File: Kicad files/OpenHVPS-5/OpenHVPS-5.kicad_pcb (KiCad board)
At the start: 2 copper layers, 40.6 x 20.8 mm, 89 parts, among them J1 Conn_01x03_Male, Q1 FQT7N10, Q2 BC846A, Q3 MMBT3906, Q4 MMBT3906, U1 MAX6008AEUR+T, U2 74HC14, U3 MAX4162, U4 CD14538BM

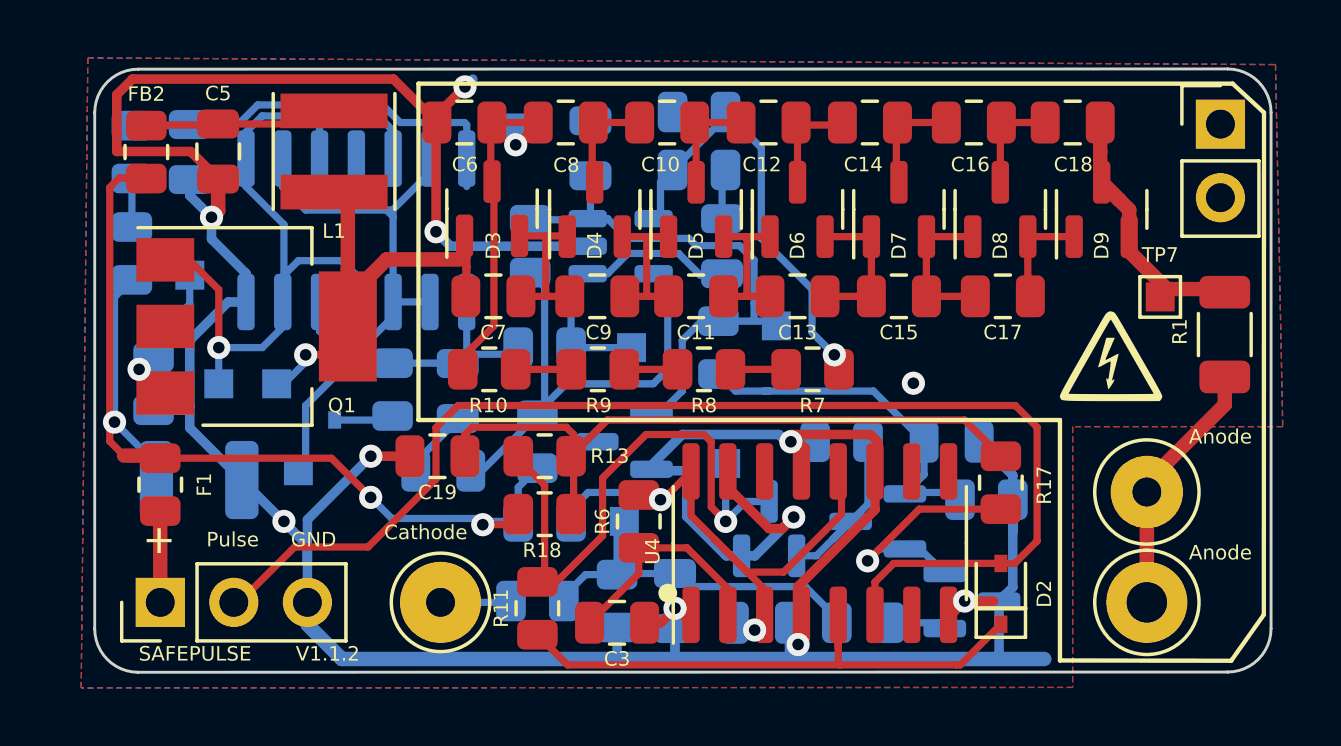
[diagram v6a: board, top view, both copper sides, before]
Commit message: Moved some lables a bit to get them centered.
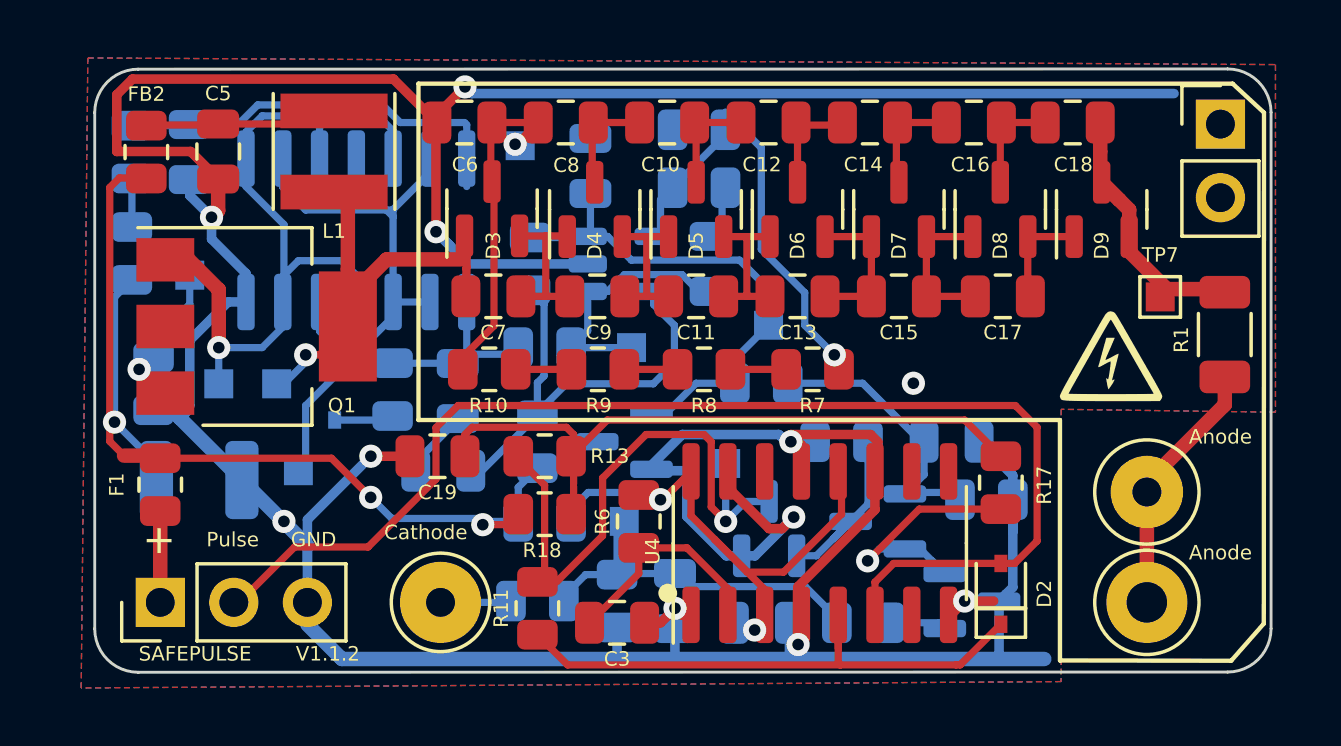
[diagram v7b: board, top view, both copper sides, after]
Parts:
- moved R14 1.92 mm to (149.2, 68.0), turned to 0 degrees
- moved C26 0.73 mm to (147.5, 63.9)
- moved C25 0.61 mm to (143.4, 60.5)
- moved R20 0.61 mm to (141.3, 63.9)
- moved R23 0.61 mm to (147.1, 59.2)
- moved R24 0.61 mm to (147.1, 61.2)
- moved TP6 0.61 mm to (140.9, 59.8)
- moved U3 0.61 mm to (144.4, 63.9)
- moved TP1 0.27 mm to (149.5, 66.0)
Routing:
- net GND: track 136.4 -> 161.5 mm
- net Net-(C24-Pad1): track 12.6 -> 9.93 mm
- net +2V5: track 19.4 -> 18.3 mm
- net Net-(C26-Pad1): track 9.77 -> 9.06 mm

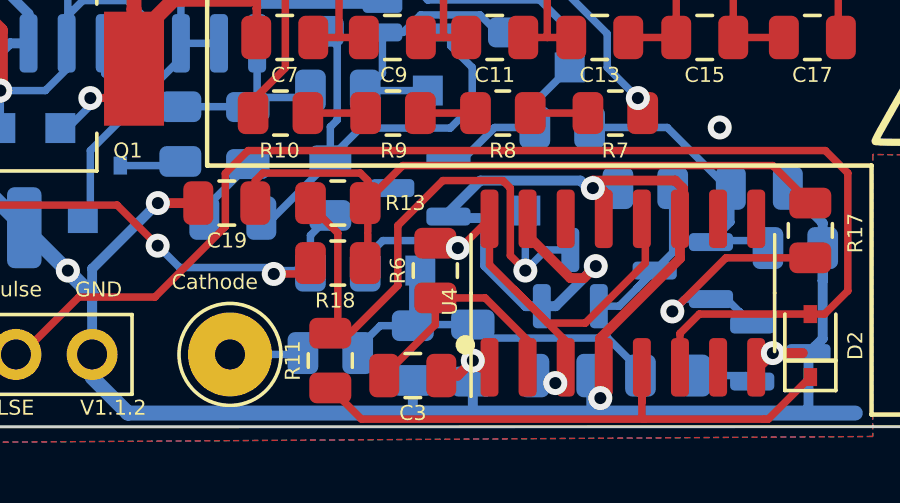
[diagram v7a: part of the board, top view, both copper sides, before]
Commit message: added digikey bom from Allan and move U4 label
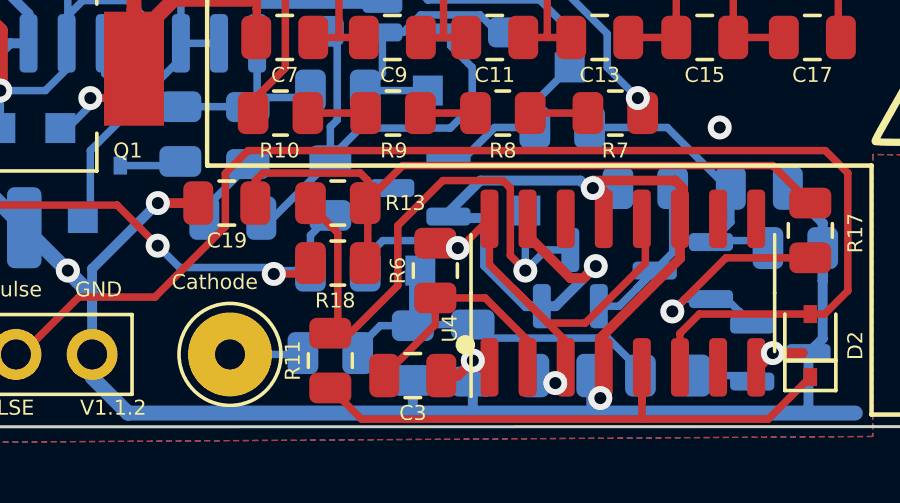
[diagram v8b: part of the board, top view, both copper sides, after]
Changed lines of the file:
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@@
     (property "Sheetname" "")
     (attr smd)
-    (fp_text reference "U4" (at -0.282 -5.767 90) (layer "F.SilkS")
+    (fp_text reference "U4" (at -1.18 -5.77 90) (layer "F.SilkS")
       (effects (font (size 0.5 0.5) (thickness 0.075)))
     )
